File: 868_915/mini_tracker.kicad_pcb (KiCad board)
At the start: 2 copper layers, 16 x 48 mm, 75 parts, among them J1 Conn_Coaxial, J2 Conn_01x05_Male, SW1 SW_DIP_x03, U1 SX1262, U2 AP2210N-3.3TRG1, U3 STM32G030F6P6, U4 SIM28ML, U5 SKY13453-385LF, Y1 NX2016SA-32MHZ-STD-CZS-5, Y2 NX2016SA-32MHZ-STD-CZS-5

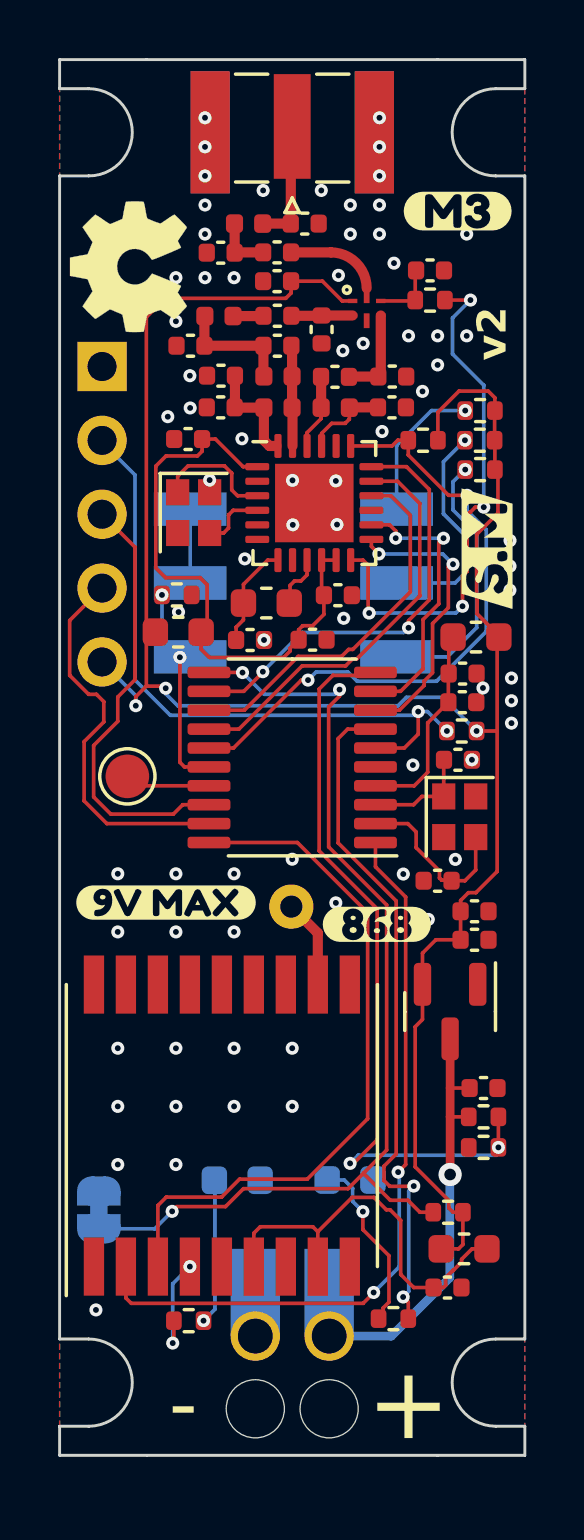
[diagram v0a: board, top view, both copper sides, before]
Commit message: Update production files
-Fixed sta and pps label swap for both versions
-Completely redesign passive network for 868 version for lower extended components fee
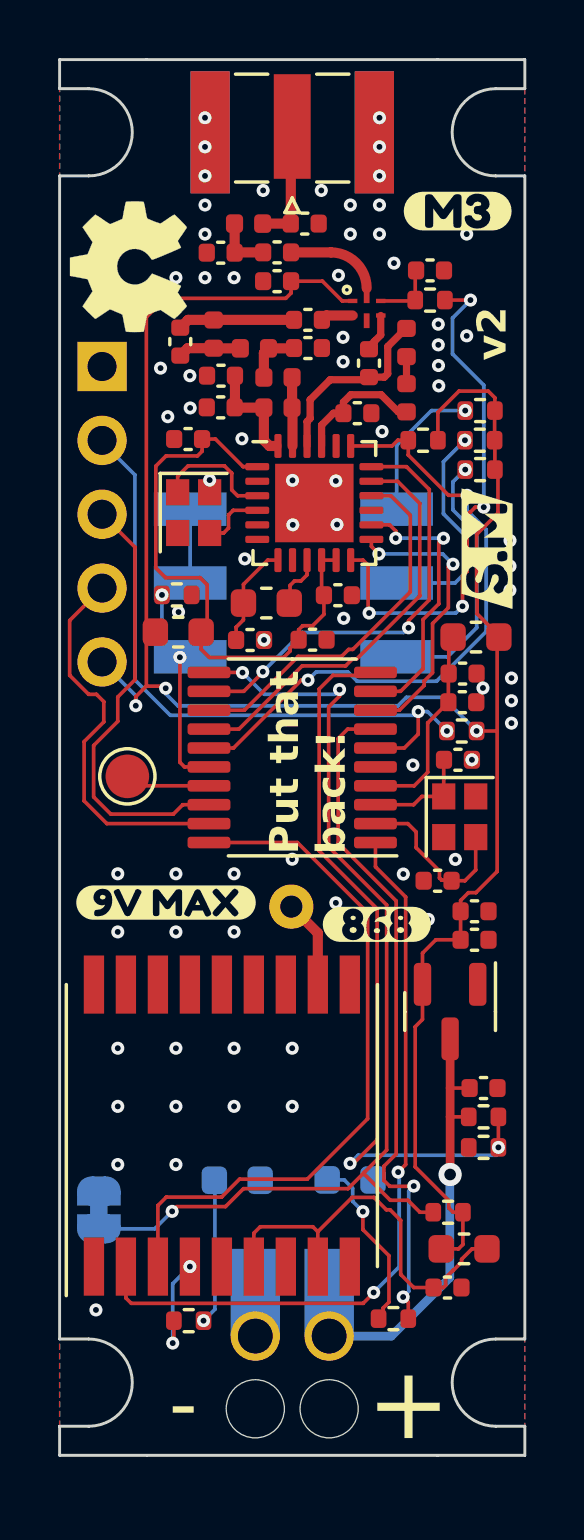
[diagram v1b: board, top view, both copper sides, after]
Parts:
- removed C12: 1pF, Capacitor_SMD:C_0402_1005Metric
- removed C13: 47pF, Capacitor_SMD:C_0402_1005Metric
- removed kibuzzard-651ADEA2: G***, kibuzzard-651ADEA2
- removed kibuzzard-651ADEAE: G***, kibuzzard-651ADEAE
- added L7: 1.3nH, Inductor_SMD:L_0402_1005Metric, F.Cu at (149.3, 91.4)
- added L8: 12nH, Inductor_SMD:L_0402_1005Metric, F.Cu at (155.9, 93.6)
- added kibuzzard-65ED95C0: G***, kibuzzard-65ED95C0, B.Cu at (154.6, 121.9)
- added kibuzzard-65ED95D2: G***, kibuzzard-65ED95D2, B.Cu at (149.8, 122.0)
- C11: value 3.6pF -> 1.5pF
- C19: value 15pF -> 5.6pF
- C21: value 9pF -> 5.6pF
- C22: value 22pF -> 100pF
- C9: value 2.7pF -> 5.6pF
- L4: value 9.1nH -> 6.5nH
- L5: value 4.3nH -> 12nH
- moved C21 4.88 mm to (148.2, 91.7), turned to -90 degrees
- moved C19 4.04 mm to (152.5, 91.9), turned to 180 degrees
- moved L3 3.32 mm to (155.9, 91.7), turned to -90 degrees
- moved L5 1.65 mm to (150.7, 91.9), turned to 180 degrees
- moved C11 1.26 mm to (154.6, 92.4), turned to 90 degrees
- moved C9 1.21 mm to (154.2, 94.2)
- moved C20 1.06 mm to (152.5, 91.0)
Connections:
- C21 pad 1: GND -> Net-(C20-Pad1)
- C21 pad 2: Net-(U5-RF1) -> Net-(C21-Pad2)
- L3 pad 2: Net-(U1-RFI_P) -> Net-(L3-Pad2)
- L5 pad 2: Net-(C20-Pad1) -> Net-(C21-Pad2)
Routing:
- net Net-(U1-RFI_N): track 2.58 -> 6.31 mm
- net Net-(C20-Pad1): track 1.05 -> 4.03 mm
- net Net-(C21-Pad2): track 0.00 -> 2.17 mm
- net Net-(C19-Pad2): track 4.11 -> 1.95 mm
- net Net-(U5-RF2): track 3.15 -> 1.33 mm
- net Net-(U1-RFI_P): track 2.97 -> 4.54 mm
- net Net-(U1-RFO): track 3.46 -> 2.36 mm
- net Net-(U5-RF1): track 2.11 -> 1.12 mm
- net Net-(L3-Pad2): track 0.00 -> 0.93 mm
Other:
- board text added: "Put that back!"
